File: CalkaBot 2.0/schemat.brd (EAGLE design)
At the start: 94.4 x 101.8 mm, 55 parts, among them IC1 TB6612FNG, IC2 LM339D, IC3 7806DT, Q1 16MHz, X1 MINI-USB-32005-301

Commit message: zmiana przycisków
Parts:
- removed BUT1, BUT2, BUT3: (no value), switch-omron:B3F-10XX
- added SW2: (no value), special:EDG-03
- moved R2 7.83 mm to (25.0, 22.7), turned to 0 degrees
- moved R6 3.47 mm to (25.0, 25.2), turned to 0 degrees
- moved C10 2.15 mm to (33.8, 29.1)
- moved R9 1.22 mm to (25.0, 27.7), turned to 0 degrees
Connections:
- net GND: now also SW2.1, SW2.2, SW2.3; no longer BUT1.1, BUT1.2, BUT2.1, BUT2.2, BUT3.1, BUT3.2
- net MISO: now also SW2.4; no longer BUT1.3, BUT1.4
- net MOSI: now also SW2.5; no longer BUT2.3, BUT2.4
- net SCK: now also SW2.6; no longer BUT3.3, BUT3.4
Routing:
- net VCC: track 297.7 -> 342.4 mm, vias 5 -> 12
- net GND: track 446.3 -> 428.0 mm, vias 5 -> 9
- net MISO: track 35.7 -> 26.7 mm
- net MOSI: track 33.1 -> 25.4 mm
- net SCK: track 29.0 -> 24.0 mm
- net UCAP: track 14.6 -> 13.1 mm
- net VM: vias 3 -> 12
- net S4: vias 2 -> 4

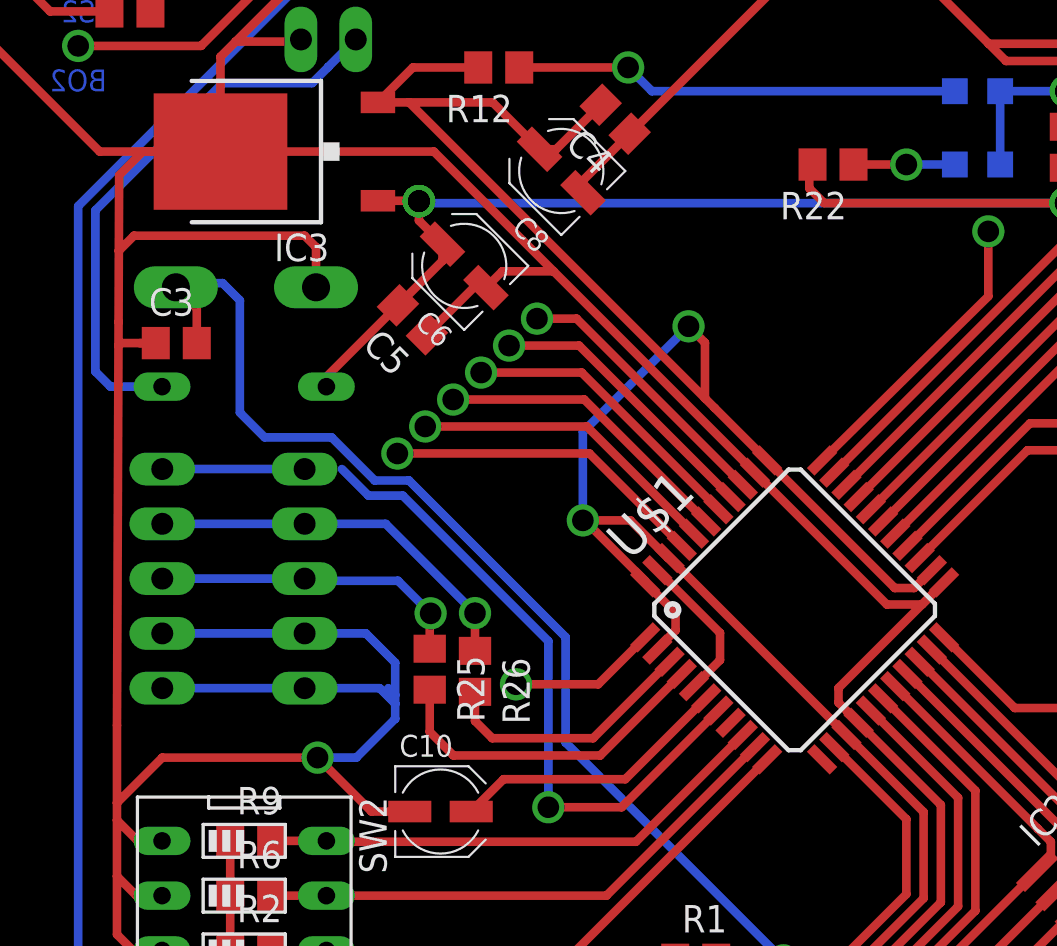
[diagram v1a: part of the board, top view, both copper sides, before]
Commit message: połączono wszystkie vcc i gnd
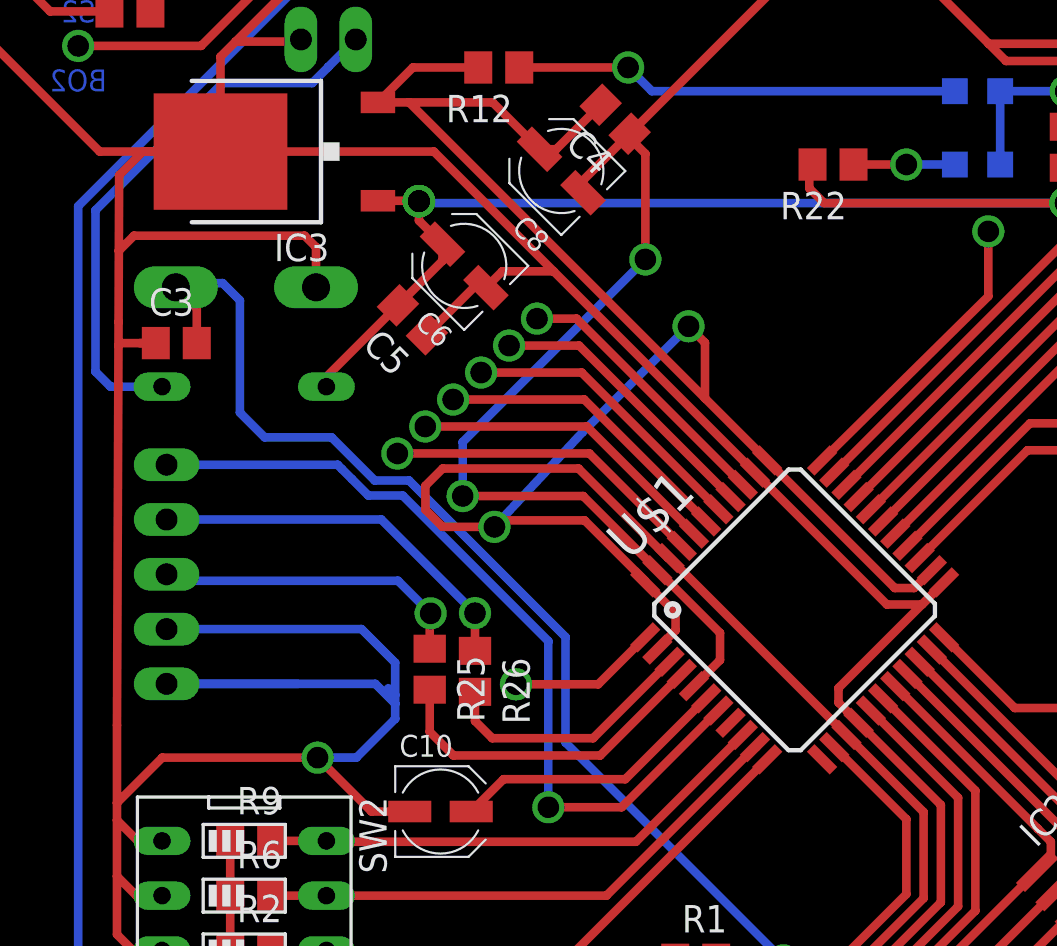
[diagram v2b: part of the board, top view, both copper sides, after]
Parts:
- removed JP3: (no value), pinhead:1X05
- moved JP2 6.40 mm to (21.1, 40.1)
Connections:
- net GND: no longer JP3.1, JP3.2
- net N$12: no longer JP3.3
- net N$20: no longer JP3.4
- net VBUS: no longer JP3.5
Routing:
- net GND: track 428.0 -> 464.9 mm, vias 9 -> 11
- net VCC: track 342.4 -> 361.8 mm
- net VBUS: track 36.9 -> 38.5 mm
